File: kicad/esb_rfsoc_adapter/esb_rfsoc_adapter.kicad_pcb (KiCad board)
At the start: 2 copper layers, 27.4 x 32.8 mm, 14 parts, among them J1 PDH Out1, J2 PDH Out0, J3 Trigger0, J4 Conn_02x06_Odd_Even, J5 Trigger1, U1 TLP2766A, U2 TLP2766A

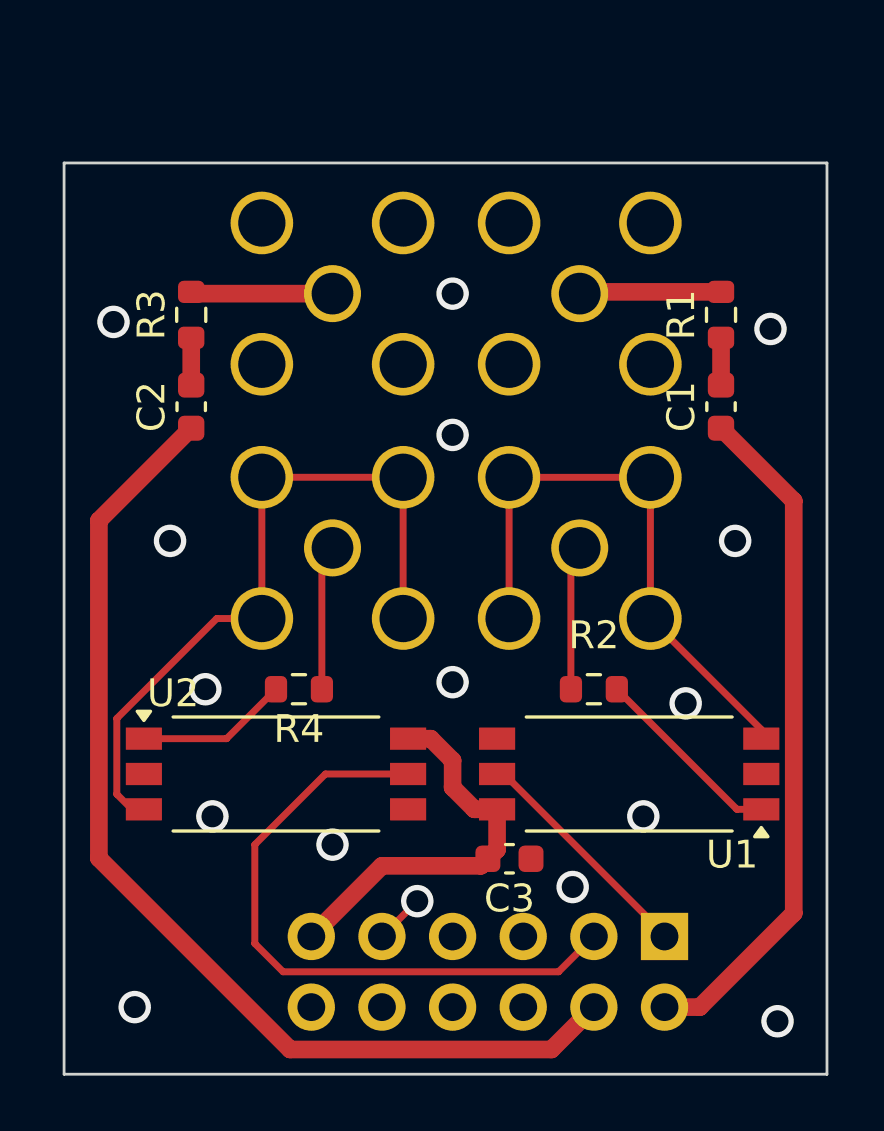
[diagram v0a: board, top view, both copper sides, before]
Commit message: On-board parser server and labscript interface updated to cooperate with the new triggering function and clock settings.
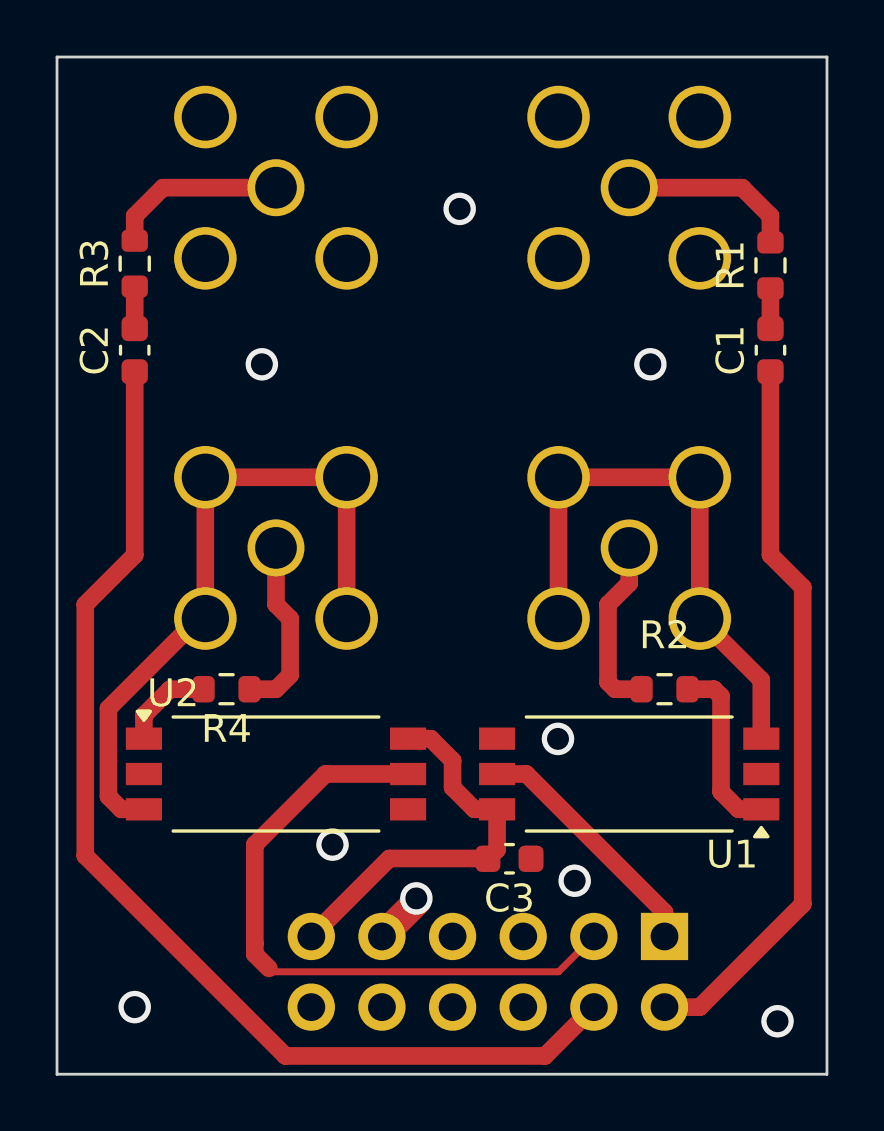
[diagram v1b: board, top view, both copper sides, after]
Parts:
- moved J1 4.32 mm to (175.3, 55.9)
- moved J2 4.20 mm to (188.0, 55.9)
- moved C2 2.87 mm to (170.2, 61.7)
- moved R3 2.74 mm to (170.2, 58.6)
- moved C1 2.70 mm to (193.0, 61.7)
- moved R4 2.60 mm to (173.5, 73.9)
- moved R2 2.54 mm to (189.2, 73.9)
- moved R1 2.51 mm to (193.0, 58.7)
- moved J5 2.03 mm to (175.3, 68.8)
- moved J3 1.78 mm to (188.0, 68.8)
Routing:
- net Net-(U2-A): track 5.49 -> 3.37 mm
- net /PMOD0_5: track 38.1 -> 40.1 mm
- net /PMOD0_4: track 24.6 -> 26.1 mm
- net Net-(J2-In): track 5.11 -> 6.45 mm
- net Net-(J1-In): track 5.11 -> 6.39 mm
- net Net-(J3-In): track 5.21 -> 6.45 mm
- net Net-(J5-In): track 5.24 -> 6.46 mm
- net Net-(J5-Ext): track 25.9 -> 24.7 mm
- net Net-(J3-Ext): track 21.2 -> 20.5 mm
- net Net-(U1-A): track 6.98 -> 6.45 mm
- net GND: vias 16 -> 9
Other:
- board size 27.4 x 32.8 mm -> 27.7 x 36.6 mm
